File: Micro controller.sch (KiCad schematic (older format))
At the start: 32 parts

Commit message: removed SD Card
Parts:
- removed J?: Micro_SD_Card, symbol Micro_SD_Card
- U1, U6: renamed from U?; footprint PJC-Sandbox:SOT23-3P95_240X120L20X48N -> micromouse:PMEG4010_DIODE
- U20: renamed from U?; footprint (none) -> micromouse:TPD3S014
- U21: renamed from U?; footprint (none) -> micromouse:MKL02Z32VFG4
- U22: renamed from U?; footprint (none) -> micromouse:LP38691
- U23: renamed from U?; footprint (none) -> micromouse:MKK66FX1M0
- Y1: renamed from Y?; footprint (none) -> micromouse:16Mhz_crystal
- Y2: renamed from Y?; footprint (none) -> micromouse:32.768_CRYSTAL
- gave numbers to parts that had none: 23
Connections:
- wire segments 121 -> 112

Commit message: generated a netlist
filled the teensy components with 0402 size untill i find out more info.
Starting to do PCB layout.
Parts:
- C16, C17, C18, C19, C20, C21, C22, C23, C24, C25, C26, C27, C28, C29, U14, U3, U5: footprint (none) -> Capacitors_SMD:C_0402
- J1: footprint (none) -> micromouse:USB_B
- R37, R38, R39, R40: footprint (none) -> Resistors_SMD:R_0402
- s1: footprint (none) -> micromouse:Switch_teensy
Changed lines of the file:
@@
 F 0 "J1" H 800 3075 50  0000 L CNN
 F 1 "USB_B" H 800 2975 50  0000 L CNN
-F 2 "" H 1150 2575 50  0001 C CNN
+F 2 "micromouse:USB_B" H 1150 2575 50  0001 C CNN
 F 3 "" H 1150 2575 50  0001 C CNN
 	1    1000 2625
@@
 F 0 "C29" H 4685 920 50  0000 L CNN
 F 1 "2.2uF" H 4685 770 50  0000 L CNN
-F 2 "" H 4675 850 50  0001 C CNN
+F 2 "Capacitors_SMD:C_0402" H 4675 850 50  0001 C CNN
 F 3 "" H 4675 850 50  0001 C CNN
 	1    4675 850
@@
 F 0 "C21" H 3560 945 50  0000 L CNN
 F 1 "0.1uF" H 3560 795 50  0000 L CNN
-F 2 "" H 3550 875 50  0001 C CNN
+F 2 "Capacitors_SMD:C_0402" H 3550 875 50  0001 C CNN
 F 3 "" H 3550 875 50  0001 C CNN
 	1    3550 875
@@
 F 0 "C16" H 1010 1470 50  0000 L CNN
 F 1 "2.2uF" H 1010 1320 50  0000 L CNN
-F 2 "" H 1000 1400 50  0001 C CNN
+F 2 "Capacitors_SMD:C_0402" H 1000 1400 50  0001 C CNN
 F 3 "" H 1000 1400 50  0001 C CNN
 	1    1000 1400
@@
 F 0 "C22" H 3660 1445 50  0000 L CNN
 F 1 "0.1uF" H 3660 1295 50  0000 L CNN
-F 2 "" H 3650 1375 50  0001 C CNN
+F 2 "Capacitors_SMD:C_0402" H 3650 1375 50  0001 C CNN
 F 3 "" H 3650 1375 50  0001 C CNN
 	1    3650 1375
@@
 F 0 "U14" H 3255 1315 39  0000 C CNN
 F 1 "ferrite" H 3150 1430 39  0000 C CNN
-F 2 "" H 3300 1475 39  0001 C CNN
+F 2 "Capacitors_SMD:C_0402" H 3300 1475 39  0001 C CNN
 F 3 "" H 3095 1285 39  0001 C CNN
 F 4 "600" H 3145 1320 39  0000 C CNN "value"
@@
 F 0 "C23" H 3985 1445 50  0000 L CNN
 F 1 "10nF" H 3985 1295 50  0000 L CNN
-F 2 "" H 3975 1375 50  0001 C CNN
+F 2 "Capacitors_SMD:C_0402" H 3975 1375 50  0001 C CNN
 F 3 "" H 3975 1375 50  0001 C CNN
 	1    3975 1375
@@
 F 0 "C25" H 4235 1445 50  0000 L CNN
 F 1 "10nF" H 4235 1295 50  0000 L CNN
-F 2 "" H 4225 1375 50  0001 C CNN
+F 2 "Capacitors_SMD:C_0402" H 4225 1375 50  0001 C CNN
 F 3 "" H 4225 1375 50  0001 C CNN
 	1    4225 1375
@@
 F 0 "C27" H 4485 1445 50  0000 L CNN
 F 1 "2.2uF" H 4485 1295 50  0000 L CNN
-F 2 "" H 4475 1375 50  0001 C CNN
+F 2 "Capacitors_SMD:C_0402" H 4475 1375 50  0001 C CNN
 F 3 "" H 4475 1375 50  0001 C CNN
 	1    4475 1375
@@
 F 0 "U3" H 2255 765 39  0000 C CNN
 F 1 "ferrite" H 2150 880 39  0000 C CNN
-F 2 "" H 2300 925 39  0001 C CNN
+F 2 "Capacitors_SMD:C_0402" H 2300 925 39  0001 C CNN
 F 3 "" H 2095 735 39  0001 C CNN
 F 4 "120" H 2145 770 39  0000 C CNN "value"
@@
 F 0 "R38" V 3905 2725 50  0000 C CNN
 F 1 "33" V 3825 2725 50  0000 C CNN
-F 2 "" V 3755 2725 50  0001 C CNN
+F 2 "Resistors_SMD:R_0402" V 3755 2725 50  0001 C CNN
 F 3 "" H 3825 2725 50  0001 C CNN
 	1    3825 2725
@@
 F 0 "R37" V 3580 2625 50  0000 C CNN
 F 1 "33" V 3500 2625 50  0000 C CNN
-F 2 "" V 3430 2625 50  0001 C CNN
+F 2 "Resistors_SMD:R_0402" V 3430 2625 50  0001 C CNN
 F 3 "" H 3500 2625 50  0001 C CNN
 	1    3500 2625
@@
 F 0 "C17" H 1760 5770 50  0000 L CNN
 F 1 "0.1uF" H 1760 5620 50  0000 L CNN
-F 2 "" H 1750 5700 50  0001 C CNN
+F 2 "Capacitors_SMD:C_0402" H 1750 5700 50  0001 C CNN
 F 3 "" H 1750 5700 50  0001 C CNN
 	1    1750 5700
@@
 F 0 "s1" H 2840 6840 60  0000 C CNN
 F 1 "Switch" H 2835 7340 60  0000 C CNN
-F 2 "" H 2825 7075 60  0001 C CNN
+F 2 "micromouse:Switch_teensy" H 2825 7075 60  0001 C CNN
 F 3 "" H 2825 7075 60  0001 C CNN
 	1    2825 7075
@@
 F 0 "U5" H 3005 2265 39  0000 C CNN
 F 1 "ferrite" H 2900 2380 39  0000 C CNN
-F 2 "" H 3050 2425 39  0001 C CNN
+F 2 "Capacitors_SMD:C_0402" H 3050 2425 39  0001 C CNN
 F 3 "" H 2845 2235 39  0001 C CNN
 F 4 "600" H 2895 2270 39  0000 C CNN "value"
@@
 F 0 "C19" H 3110 2095 50  0000 L CNN
 F 1 "2.2uF" H 3110 1945 50  0000 L CNN
-F 2 "" H 3100 2025 50  0001 C CNN
+F 2 "Capacitors_SMD:C_0402" H 3100 2025 50  0001 C CNN
 F 3 "" H 3100 2025 50  0001 C CNN
 	1    3100 2025
@@
 F 0 "R39" V 3930 1925 50  0000 C CNN
 F 1 "470" V 3850 1925 50  0000 C CNN
-F 2 "" V 3780 1925 50  0001 C CNN
+F 2 "Resistors_SMD:R_0402" V 3780 1925 50  0001 C CNN
 F 3 "" H 3850 1925 50  0001 C CNN
 	1    3850 1925
@@
 F 0 "C28" H 4660 2245 50  0000 L CNN
 F 1 "0.1uF" H 4660 2095 50  0000 L CNN
-F 2 "" H 4650 2175 50  0001 C CNN
+F 2 "Capacitors_SMD:C_0402" H 4650 2175 50  0001 C CNN
 F 3 "" H 4650 2175 50  0001 C CNN
 	1    4650 2175
@@
 F 0 "C26" H 4285 2245 50  0000 L CNN
 F 1 "0.1uF" H 4285 2095 50  0000 L CNN
-F 2 "" H 4275 2175 50  0001 C CNN
+F 2 "Capacitors_SMD:C_0402" H 4275 2175 50  0001 C CNN
 F 3 "" H 4275 2175 50  0001 C CNN
 	1    4275 2175
@@
 F 0 "R40" V 4555 3825 50  0000 C CNN
 F 1 "100k" V 4475 3825 50  0000 C CNN
-F 2 "" V 4405 3825 50  0001 C CNN
+F 2 "Resistors_SMD:R_0402" V 4405 3825 50  0001 C CNN
 F 3 "" H 4475 3825 50  0001 C CNN
 	1    4475 3825
@@
 F 0 "C20" H 3160 3620 50  0000 L CNN
 F 1 "100uF" H 3160 3470 50  0000 L CNN
-F 2 "" H 3150 3550 50  0001 C CNN
+F 2 "Capacitors_SMD:C_0402" H 3150 3550 50  0001 C CNN
 F 3 "" H 3150 3550 50  0001 C CNN
 	1    3150 3550
@@
 F 0 "C18" H 2335 4470 50  0000 L CNN
 F 1 "2.2uF" H 2335 4320 50  0000 L CNN
-F 2 "" H 2325 4400 50  0001 C CNN
+F 2 "Capacitors_SMD:C_0402" H 2325 4400 50  0001 C CNN
 F 3 "" H 2325 4400 50  0001 C CNN
 	1    2325 4400
@@
 F 0 "C24" H 4210 3570 50  0000 L CNN
 F 1 "2.2uF" H 4210 3420 50  0000 L CNN
-F 2 "" H 4200 3500 50  0001 C CNN
+F 2 "Capacitors_SMD:C_0402" H 4200 3500 50  0001 C CNN
 F 3 "" H 4200 3500 50  0001 C CNN
 	1    4200 3500

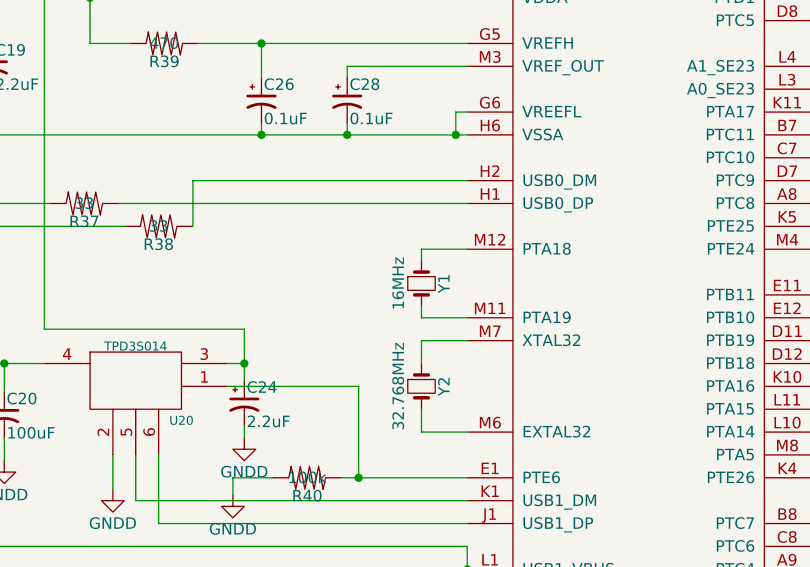
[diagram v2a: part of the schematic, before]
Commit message: Added MPU-6500
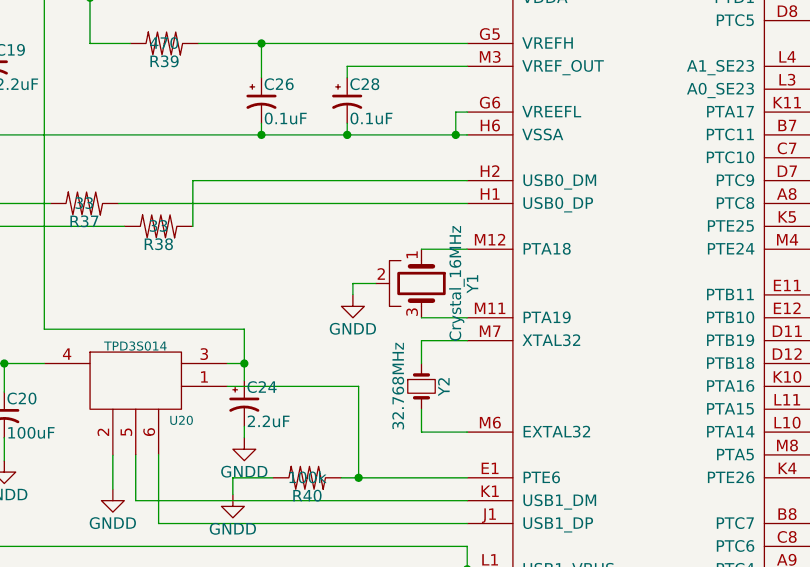
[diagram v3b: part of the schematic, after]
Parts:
- removed Y1: 16MHz, micromouse:16Mhz_crystal, symbol Crystal_Small
- added Y1: Crystal_16MHz, micromouse:16Mhz_crystal, symbol Crystal_GND2
- C20: footprint Capacitors_SMD:C_0402 -> Capacitors_SMD:C_1206
- U23: footprint micromouse:MKK66FX1M0 -> micromouse:Microcontroller
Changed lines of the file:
@@
 EESchema Schematic File Version 2
+LIBS:device
+LIBS:Micromouse
 LIBS:power
-LIBS:device
 LIBS:transistors
 LIBS:conn
@@
 LIBS:contrib
 LIBS:valves
-LIBS:Micromouse
 LIBS:1_PJC-Sandbox
 LIBS:Micromouse1.2-cache
@@
 $Descr A4 11693 8268
 encoding utf-8
-Sheet 6 7
+Sheet 6 8
 Title ""
 Date ""
@@
 F 0 "U23" H 5975 225 39  0000 C CNN
 F 1 "MK66FX1M0" H 5875 6975 39  0000 C CNN
-F 2 "micromouse:MKK66FX1M0" H 5775 3825 39  0001 C CNN
+F 2 "micromouse:Microcontroller" H 5775 3825 39  0001 C CNN
 F 3 "" H 5775 3825 39  0001 C CNN
 F 4 "." H 6075 325 39  0000 C CNN "manf#"
@@
 $EndComp
 $Comp
-L GND #PWR015
+L GND #PWR013
 U 1 1 594A0755
 P 4025 1050
-F 0 "#PWR015" H 4025 800 50  0001 C CNN
+F 0 "#PWR013" H 4025 800 50  0001 C CNN
 F 1 "GND" H 4025 900 50  0000 C CNN
 F 2 "" H 4025 1050 50  0001 C CNN
@@
 $EndComp
 $Comp
-L GND #PWR016
+L GND #PWR014
 U 1 1 594A079F
 P 4225 1050
-F 0 "#PWR016" H 4225 800 50  0001 C CNN
+F 0 "#PWR014" H 4225 800 50  0001 C CNN
 F 1 "GND" H 4225 900 50  0000 C CNN
 F 2 "" H 4225 1050 50  0001 C CNN
@@
 $EndComp
 $Comp
-L GND #PWR017
+L GND #PWR015
 U 1 1 594A0864
 P 4675 1000
-F 0 "#PWR017" H 4675 750 50  0001 C CNN
+F 0 "#PWR015" H 4675 750 50  0001 C CNN
 F 1 "GND" H 4675 850 50  0000 C CNN
 F 2 "" H 4675 1000 50  0001 C CNN
@@
 $EndComp
 $Comp
-L GND #PWR018
+L GND #PWR016
 U 1 1 594A0891
 P 3550 1050
-F 0 "#PWR018" H 3550 800 50  0001 C CNN
+F 0 "#PWR016" H 3550 800 50  0001 C CNN
 F 1 "GND" H 3550 900 50  0000 C CNN
 F 2 "" H 3550 1050 50  0001 C CNN
@@
 $EndComp
 $Comp
-L GNDD #PWR019
+L GNDD #PWR017
 U 1 1 594A0F24
 P 1000 1600
-F 0 "#PWR019" H 1000 1350 50  0001 C CNN
+F 0 "#PWR017" H 1000 1350 50  0001 C CNN
 F 1 "GNDD" H 1000 1450 50  0000 C CNN
 F 2 "" H 1000 1600 50  0001 C CNN
@@
 $EndComp
 $Comp
-L GND #PWR020
+L GND #PWR018
 U 1 1 594A19D2
 P 4475 1550
-F 0 "#PWR020" H 4475 1300 50  0001 C CNN
+F 0 "#PWR018" H 4475 1300 50  0001 C CNN
 F 1 "GND" H 4475 1400 50  0000 C CNN
 F 2 "" H 4475 1550 50  0001 C CNN
@@
 $EndComp
 $Comp
-L GND #PWR021
+L GND #PWR019
 U 1 1 594A1F04
 P 900 3125
-F 0 "#PWR021" H 900 2875 50  0001 C CNN
+F 0 "#PWR019" H 900 2875 50  0001 C CNN
 F 1 "GND" H 900 2975 50  0000 C CNN
 F 2 "" H 900 3125 50  0001 C CNN
@@
 $EndComp
 $Comp
-L GNDD #PWR022
+L GNDD #PWR020
 U 1 1 594A2D63
 P 4900 7400
-F 0 "#PWR022" H 4900 7150 50  0001 C CNN
+F 0 "#PWR020" H 4900 7150 50  0001 C CNN
 F 1 "GNDD" H 4900 7250 50  0000 C CNN
 F 2 "" H 4900 7400 50  0001 C CNN
@@
 $EndComp
 $Comp
-L GNDD #PWR023
+L GNDD #PWR021
 U 1 1 594A3CA9
 P 1750 5875
-F 0 "#PWR023" H 1750 5625 50  0001 C CNN
+F 0 "#PWR021" H 1750 5625 50  0001 C CNN
 F 1 "GNDD" H 1750 5725 50  0000 C CNN
 F 2 "" H 1750 5875 50  0001 C CNN
@@
 $EndComp
 $Comp
-L GNDD #PWR024
+L GNDD #PWR022
 U 1 1 594A4083
 P 3100 7350
-F 0 "#PWR024" H 3100 7100 50  0001 C CNN
+F 0 "#PWR022" H 3100 7100 50  0001 C CNN
 F 1 "GNDD" H 3100 7200 50  0000 C CNN
 F 2 "" H 3100 7350 50  0001 C CNN
@@
 $EndComp
 $Comp
-L GNDD #PWR025
+L GNDD #PWR023
 U 1 1 594A40CA
 P 2825 7350
-F 0 "#PWR025" H 2825 7100 50  0001 C CNN
+F 0 "#PWR023" H 2825 7100 50  0001 C CNN
 F 1 "GNDD" H 2825 7200 50  0000 C CNN
 F 2 "" H 2825 7350 50  0001 C CNN
@@
 $EndComp
 $Comp
-L GNDD #PWR026
+L GNDD #PWR024
 U 1 1 594A46C4
 P 2550 2500
-F 0 "#PWR026" H 2550 2250 50  0001 C CNN
+F 0 "#PWR024" H 2550 2250 50  0001 C CNN
 F 1 "GNDD" H 2550 2350 50  0000 C CNN
 F 2 "" H 2550 2500 50  0001 C CNN
@@
 $EndComp
 $Comp
-L Crystal_Small Y1
-U 1 1 594A56BE
-P 4975 2975
-F 0 "Y1" H 4975 3075 50  0000 C CNN
-F 1 "16MHz" H 4975 2875 50  0000 C CNN
-F 2 "micromouse:16Mhz_crystal" H 4975 2975 50  0001 C CNN
-F 3 "" H 4975 2975 50  0001 C CNN
-	1    4975 2975
-	0    1    1    0
-$EndComp
-$Comp
 L Crystal_Small Y2
 U 1 1 594A5756
@@
 $EndComp
 $Comp
-L GNDD #PWR027
+L GNDD #PWR025
 U 1 1 594A5B36
 P 4150 3900
-F 0 "#PWR027" H 4150 3650 50  0001 C CNN
+F 0 "#PWR025" H 4150 3650 50  0001 C CNN
 F 1 "GNDD" H 4150 3750 50  0000 C CNN
 F 2 "" H 4150 3900 50  0001 C CNN
@@
 Connection ~ 5125 2325
 Wire Wire Line
-	5175 2825 4975 2825
-Wire Wire Line
-	4975 2825 4975 2875
-Wire Wire Line
-	5175 3125 4975 3125
-Wire Wire Line
-	4975 3125 4975 3075
-Wire Wire Line
 	5175 3225 4975 3225
 Wire Wire Line
@@
 F 0 "C20" H 3160 3620 50  0000 L CNN
 F 1 "100uF" H 3160 3470 50  0000 L CNN
-F 2 "Capacitors_SMD:C_0402" H 3150 3550 50  0001 C CNN
+F 2 "Capacitors_SMD:C_1206" H 3150 3550 50  0001 C CNN
 F 3 "" H 3150 3550 50  0001 C CNN
 	1    3150 3550
@@
 $EndComp
 $Comp
-L GNDD #PWR028
+L GNDD #PWR026
 U 1 1 594A6698
 P 3150 3750
-F 0 "#PWR028" H 3150 3500 50  0001 C CNN
+F 0 "#PWR026" H 3150 3500 50  0001 C CNN
 F 1 "GNDD" H 3150 3600 50  0000 C CNN
 F 2 "" H 3150 3750 50  0001 C CNN
@@
 	3150 3650 3150 3750
 $Comp
-L GNDD #PWR029
+L GNDD #PWR027
 U 1 1 594A68B7
 P 3625 3875
-F 0 "#PWR029" H 3625 3625 50  0001 C CNN
+F 0 "#PWR027" H 3625 3625 50  0001 C CNN
 F 1 "GNDD" H 3625 3725 50  0000 C CNN
 F 2 "" H 3625 3875 50  0001 C CNN
@@
 Connection ~ 2325 4125
 $Comp
-L GNDD #PWR030
+L GNDD #PWR028
 U 1 1 594A75BB
 P 2325 4575
-F 0 "#PWR030" H 2325 4325 50  0001 C CNN
+F 0 "#PWR028" H 2325 4325 50  0001 C CNN
 F 1 "GNDD" H 2325 4425 50  0000 C CNN
 F 2 "" H 2325 4575 50  0001 C CNN
@@
 $EndComp
 $Comp
-L GNDD #PWR031
+L GNDD #PWR029
 U 1 1 594A7E36
 P 4200 3650
-F 0 "#PWR031" H 4200 3400 50  0001 C CNN
+F 0 "#PWR029" H 4200 3400 50  0001 C CNN
 F 1 "GNDD" H 4200 3500 50  0000 C CNN
 F 2 "" H 4200 3650 50  0001 C CNN
@@
 Wire Wire Line
 	2075 4200 1850 4200
+$Comp
+L Crystal_GND2 Y1
+U 1 1 59891C87
+P 4975 2975
+F 0 "Y1" H 4975 3200 50  0000 C CNN
+F 1 "Crystal_16MHz" H 4975 3125 50  0000 C CNN
+F 2 "micromouse:16Mhz_crystal" H 4975 2975 50  0001 C CNN
+F 3 "" H 4975 2975 50  0001 C CNN
+	1    4975 2975
+	0    1    1    0
+$EndComp
+Wire Wire Line
+	4975 2825 5175 2825
+Wire Wire Line
+	5175 3125 4975 3125
+$Comp
+L GNDD #PWR030
+U 1 1 598926F4
+P 4675 3025
+F 0 "#PWR030" H 4675 2775 50  0001 C CNN
+F 1 "GNDD" H 4675 2875 50  0000 C CNN
+F 2 "" H 4675 3025 50  0001 C CNN
+F 3 "" H 4675 3025 50  0001 C CNN
+	1    4675 3025
+	1    0    0    -1
+$EndComp
+Wire Wire Line
+	4775 2975 4675 2975
+Wire Wire Line
+	4675 2975 4675 3025
 $EndSCHEMATC

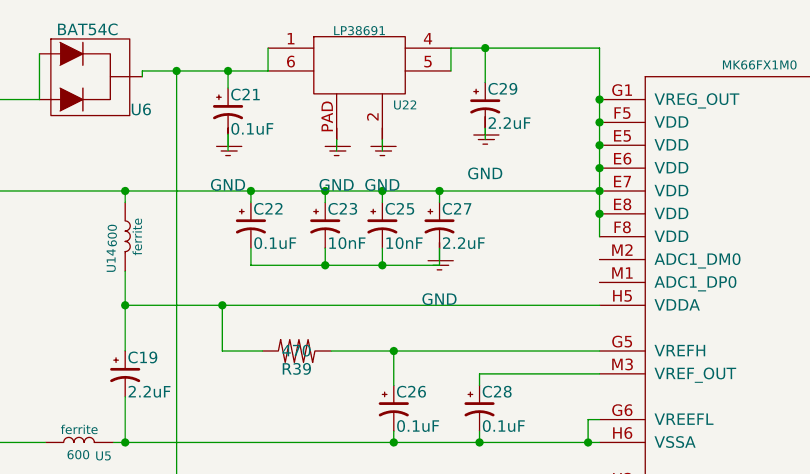
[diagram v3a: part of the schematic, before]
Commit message: finished floor planning
-replaced the TC4427 and H brige by a single DRV8833 chip
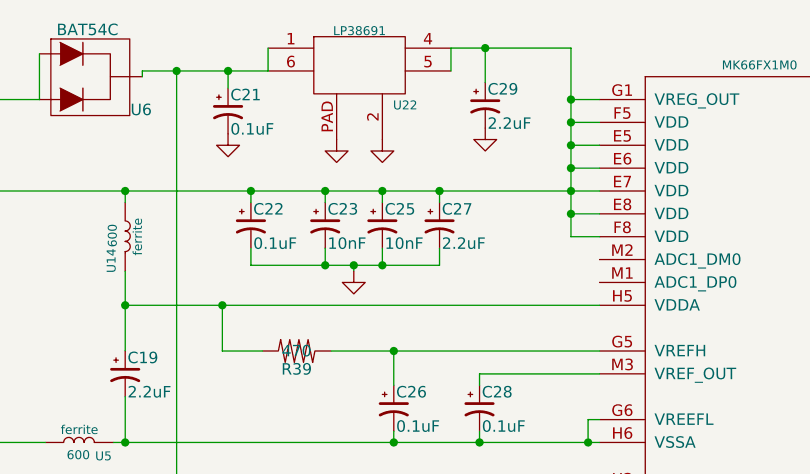
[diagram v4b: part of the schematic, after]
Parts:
- C16, C18, C19, C24, C27, C29, U3: footprint Capacitors_SMD:C_0402 -> micromouse:C_0603
- C17, C21, C22, C23, C25, C26, C28: footprint Capacitors_SMD:C_0402 -> micromouse:C_0402
- C20: footprint Capacitors_SMD:C_1206 -> micromouse:C_1206
- J1: footprint micromouse:USB_B -> micromouse:USB_Micro-B
- R39, R40: footprint Resistors_SMD:R_0402 -> micromouse:R_0402
- U14, U5: footprint Capacitors_SMD:C_0402 -> micromouse:R_0402
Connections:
- wire segments 112 -> 115
